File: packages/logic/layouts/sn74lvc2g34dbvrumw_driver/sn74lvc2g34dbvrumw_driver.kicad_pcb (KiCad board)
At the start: 2 copper layers, 2 parts

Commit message: WIP update logic
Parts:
- C1: footprint atopile:C0402-b3ef17 -> Samsung_Electro_Mechanics_CL05B104KO5NNNC:C0402
- U1: footprint atopile:SOT-23-6_L2.9-W1.6-P0.95-LS2.8-BR-bfc73b -> UMW_SN74LVC2G34DBVR_UMW:SOT-23-6_L2.9-W1.6-P0.95-LS2.8-BR
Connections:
- U1 pad 1: line-1 -> line
- U1 pad 4: line-3 -> line-1
- U1 pad 6: line -> line-3
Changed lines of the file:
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@@
     (net 0 "")
     (net 7 "VCC")
-    (net 8 "line-1")
+    (net 8 "line")
     (net 9 "gnd")
-    (net 10 "line")
+    (net 10 "line-3")
     (net 11 "line-2")
-    (net 12 "line-3")
-    (footprint "atopile:C0402-b3ef17"
+    (net 12 "line-1")
+    (footprint "Samsung_Electro_Mechanics_CL05B104KO5NNNC:C0402"
         (layer "F.Cu")
         (at -3.5 0 180)
@@
             )
         )
-        (property "Datasheet" ""
+        (property "Datasheet" "https://www.lcsc.com/datasheet/lcsc_datasheet_2304140030_Samsung-Electro-Mechanics-CL05B104KO5NNNC_C1525.pdf"
             (at 0 0 0)
             (layer "F.Fab")
@@
             )
         )
-        (property "__atopile_lib_fp_hash__" "ef4a2faf-85b3-7ef1-eb8e-b02118ddfcb4"
+        (property "__atopile_lib_fp_hash__" "a8dda1fb-951b-1ec9-ddcd-1be02a19fa0b"
             (at 0 0 0)
             (layer "User.9")
@@
             )
         )
+        (property "checksum" "6defc2b2ec38bb2969880252ed576d3bdeb093dc3bff2a0e0428d940391a2a4b"
+            (at 0 0 0)
+            (layer "User.9")
+            (hide no)
+            (effects
+                (font
+                    (size 0.125 0.125)
+                    (thickness 0.01875)
+                )
+                (hide yes)
+            )
+        )
         (attr smd)
+        (fp_line
+            (start 1.02 -0.5)
+            (end 0.23 -0.5)
+            (stroke
+                (width 0.15)
+                (type solid)
+            )
+            (layer "F.SilkS")
+        )
+        (fp_line
+            (start 0.23 0.5)
+            (end 1.02 0.5)
+            (stroke
+                (width 0.15)
+                (type solid)
+            )
+            (layer "F.SilkS")
+        )
         (fp_line
             (start 1.17 0.35)
@@
         )
         (fp_line
-            (start 1.02 -0.5)
-            (end 0.23 -0.5)
-            (stroke
-                (width 0.15)
-                (type solid)
-            )
-            (layer "F.SilkS")
-        )
-        (fp_line
-            (start 0.23 0.5)
-            (end 1.02 0.5)
+            (start -1.02 -0.5)
+            (end -0.23 -0.5)
             (stroke
                 (width 0.15)
@@
         )
         (fp_line
-            (start -1.02 -0.5)
-            (end -0.23 -0.5)
-            (stroke
-                (width 0.15)
-                (type solid)
-            )
-            (layer "F.SilkS")
-        )
-        (fp_line
             (start -1.17 0.35)
             (end -1.17 -0.35)
@@
         (fp_arc
             (start 1.17 0.35)
-            (mid 1.126066 0.456066)
-            (end 1.02 0.5)
+            (mid 1.1260660171779822 0.456066017177982)
+            (end 1.02 0.4999999999999999)
             (stroke
                 (width 0.15)
@@
         (fp_arc
             (start 1.02 -0.5)
-            (mid 1.126066 -0.456066)
+            (mid 1.1260660171779822 -0.4560660171779821)
             (end 1.17 -0.35)
             (stroke
@@
         )
         (fp_arc
-            (start -1.02 0.5)
-            (mid -1.126066 0.456066)
-            (end -1.17 0.35)
+            (start -1.17 0.35)
+            (mid -1.1260660171779822 0.456066017177982)
+            (end -1.02 0.4999999999999999)
             (stroke
                 (width 0.15)
@@
         )
         (fp_arc
-            (start -1.17 -0.35)
-            (mid -1.126066 -0.456066)
-            (end -1.02 -0.5)
+            (start -1.02 -0.5)
+            (mid -1.1260660171779822 -0.4560660171779821)
+            (end -1.17 -0.35)
             (stroke
                 (width 0.15)
@@
             (layer "F.Fab")
         )
+        (fp_text user "%R"
+            (at 0 0 0)
+            (layer "F.Fab")
+            (effects
+                (font
+                    (size 1 1)
+                    (thickness 0.15)
+                )
+            )
+            (unlocked no)
+        )
         (fp_text user "${REFERENCE}"
-            (at 0 0 0)
-            (layer "F.Fab")
+            (at 0 -4 0)
+            (layer "F.SilkS")
             (effects
                 (font
@@
             )
             (unlocked no)
+        )
+        (pad "2" smd rect
+            (at 0.55 0 180)
+            (size 0.79 0.54)
+            (layers "F.Cu" "F.Paste" "F.Mask")
+            (net 9 "gnd")
         )
         (pad "1" smd rect
             (at -0.55 0 180)
             (size 0.79 0.54)
-            (layers "F.Cu" "F.Mask" "F.Paste")
+            (layers "F.Cu" "F.Paste" "F.Mask")
             (net 7 "VCC")
         )
-        (pad "2" smd rect
-            (at 0.55 0 180)
-            (size 0.79 0.54)
-            (layers "F.Cu" "F.Mask" "F.Paste")
-            (net 9 "gnd")
-        )
-        (embedded_fonts no)
+        (model "${KIPRJMOD}/../../parts/Samsung_Electro_Mechanics_CL05B104KO5NNNC/C0402_L1.0-W0.5-H0.5.step"
+            (offset
+                (xyz 0 0 0)
+            )
+            (scale
+                (xyz 1 1 1)
+            )
+            (rotate
+                (xyz 0 0 0)
+            )
+        )
     )
-    (footprint "atopile:SOT-23-6_L2.9-W1.6-P0.95-LS2.8-BR-bfc73b"
+    (footprint "UMW_SN74LVC2G34DBVR_UMW:SOT-23-6_L2.9-W1.6-P0.95-LS2.8-BR"
         (layer "F.Cu")
         (at 0 0 0)
@@
                     (thickness 0.15)
                 )
-                (hide yes)
             )
         )
@@
             )
         )
-        (property "__atopile_lib_fp_hash__" "7cd08ec5-0e67-1657-3d93-8dff281e4252"
+        (property "__atopile_lib_fp_hash__" "1349fb2a-c60f-22cc-0534-77da642b2d35"
             (at 0 0 0)
             (layer "User.9")
@@
                     (thickness 0.01875)
                 )
+            )
+        )
+        (property "checksum" "90c74f2781f446a0c322669d965f531dd418a618657f545bd3f6b8b0b60fa378"
+            (at 0 0 0)
+            (layer "User.9")
+            (hide no)
+            (effects
+                (font
+                    (size 0.125 0.125)
+                    (thickness 0.01875)
+                )
+                (hide yes)
             )
         )
@@
             (size 1.1 0.6)
             (layers "F.Cu" "F.Paste" "F.Mask")
-            (net 8 "line-1")
+            (net 8 "line")
         )
         (pad "6" smd rect
@@
             (size 1.1 0.6)
             (layers "F.Cu" "F.Paste" "F.Mask")
-            (net 10 "line")
+            (net 10 "line-3")
         )
         (pad "5" smd rect
@@
             (size 1.1 0.6)
             (layers "F.Cu" "F.Paste" "F.Mask")
-            (net 12 "line-3")
-        )
-        (model "/home/ruben/Documents/repos/atopile_projects/Apps/ato-library/packages/logic/build/kicad/libs/lcsc.3dshapes/SOT-23-6_L2.9-W1.6-H1.5-LS2.8-P0.95.wrl"
+            (net 12 "line-1")
+        )
+        (model "${KIPRJMOD}/../../parts/UMW_SN74LVC2G34DBVR_UMW/SOT-23-6_L2.9-W1.6-H1.5-LS2.8-P0.95.step"
             (offset
                 (xyz 0 0 0)

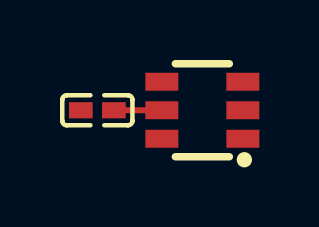
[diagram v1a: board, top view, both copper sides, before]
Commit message: Update 3D model locations
fix missing renders
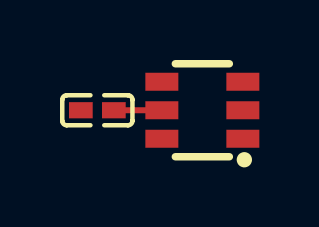
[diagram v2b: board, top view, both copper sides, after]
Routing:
- net VCC: track 0.00 -> 1.60 mm
- net (no net): track 1.60 -> 0.00 mm

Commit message: rebuild all packages & regenerate images of changed layouts (silk)
Add new scripts for version bump and build (based on atopile/packages)
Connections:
- U1 pad 3: line-2 -> line-1
- U1 pad 4: line-1 -> line-3
- U1 pad 6: line-3 -> line-2
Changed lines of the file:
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@@
     (net 2 "line")
     (net 3 "gnd")
-    (net 4 "line-3")
-    (net 5 "line-2")
-    (net 6 "line-1")
+    (net 4 "line-2")
+    (net 5 "line-1")
+    (net 6 "line-3")
     (footprint "UMW_SN74LVC2G34DBVR_UMW:SOT-23-6_L2.9-W1.6-P0.95-LS2.8-BR"
         (layer "F.Cu")
@@
             )
         )
-        (property "__atopile_lib_fp_hash__" "1349fb2a-c60f-22cc-0534-77da642b2d35"
+        (property "__atopile_lib_fp_hash__" "50ac2c3c-bf16-be49-574d-6dfde1c4a470"
             (at 0 0 0)
             (layer "User.9")
@@
             )
         )
-        (property "checksum" "90c74f2781f446a0c322669d965f531dd418a618657f545bd3f6b8b0b60fa378"
-            (at 0 0 0)
-            (layer "User.9")
-            (hide yes)
-            (effects
-                (font
-                    (size 0.125 0.125)
-                    (thickness 0.01875)
-                )
+        (property "checksum" "6bc27c223c43a0951c7a317be577427d2176831fcb6a64a0bd8550f595544d12"
+            (at 0 0 0)
+            (layer "User.9")
+            (hide no)
+            (effects
+                (font
+                    (size 0.125 0.125)
+                    (thickness 0.01875)
+                )
+                (hide yes)
             )
         )
@@
         )
         (fp_circle
-            (center 1.4 1.65)
-            (end 1.53 1.65)
-            (stroke
-                (width 0.25)
+            (center 1.4 1.45)
+            (end 1.43 1.45)
+            (stroke
+                (width 0.06)
                 (type solid)
             )
             (fill no)
-            (layer "F.SilkS")
+            (layer "F.Fab")
         )
         (fp_circle
@@
         )
         (fp_circle
-            (center 1.4 1.45)
-            (end 1.43 1.45)
-            (stroke
-                (width 0.06)
+            (center 1.4 1.65)
+            (end 1.53 1.65)
+            (stroke
+                (width 0.25)
                 (type solid)
             )
             (fill no)
-            (layer "F.Fab")
+            (layer "F.SilkS")
+        )
+        (fp_text user "%R"
+            (at 0 0 0)
+            (layer "F.Fab")
+            (effects
+                (font
+                    (size 1 1)
+                    (thickness 0.15)
+                )
+            )
+            (unlocked no)
         )
         (fp_text user "${REFERENCE}"
-            (at 0 0 0)
-            (layer "F.Fab")
+            (at 0 -4.95 0)
+            (layer "F.SilkS")
             (effects
                 (font
@@
             )
             (unlocked no)
+        )
+        (pad "3" smd rect
+            (at 1.35 -0.95 0)
+            (size 1.1 0.6)
+            (layers "F.Cu" "F.Paste" "F.Mask")
+            (net 5 "line-1")
+        )
+        (pad "2" smd rect
+            (at 1.35 0 0)
+            (size 1.1 0.6)
+            (layers "F.Cu" "F.Paste" "F.Mask")
+            (net 3 "gnd")
         )
         (pad "1" smd rect
             (at 1.35 0.95 0)
             (size 1.1 0.6)
-            (layers "F.Cu" "F.Mask" "F.Paste")
+            (layers "F.Cu" "F.Paste" "F.Mask")
             (net 2 "line")
         )
-        (pad "2" smd rect
-            (at 1.35 0 0)
-            (size 1.1 0.6)
-            (layers "F.Cu" "F.Mask" "F.Paste")
-            (net 3 "gnd")
-        )
-        (pad "3" smd rect
-            (at 1.35 -0.95 0)
-            (size 1.1 0.6)
-            (layers "F.Cu" "F.Mask" "F.Paste")
-            (net 5 "line-2")
+        (pad "6" smd rect
+            (at -1.35 0.95 0)
+            (size 1.1 0.6)
+            (layers "F.Cu" "F.Paste" "F.Mask")
+            (net 4 "line-2")
+        )
+        (pad "5" smd rect
+            (at -1.35 0 0)
+            (size 1.1 0.6)
+            (layers "F.Cu" "F.Paste" "F.Mask")
+            (net 1 "VCC")
         )
         (pad "4" smd rect
             (at -1.35 -0.95 0)
             (size 1.1 0.6)
-            (layers "F.Cu" "F.Mask" "F.Paste")
-            (net 6 "line-1")
-        )
-        (pad "5" smd rect
-            (at -1.35 0 0)
-            (size 1.1 0.6)
-            (layers "F.Cu" "F.Mask" "F.Paste")
-            (net 1 "VCC")
-        )
-        (pad "6" smd rect
-            (at -1.35 0.95 0)
-            (size 1.1 0.6)
-            (layers "F.Cu" "F.Mask" "F.Paste")
-            (net 4 "line-3")
-        )
-        (embedded_fonts no)
+            (layers "F.Cu" "F.Paste" "F.Mask")
+            (net 6 "line-3")
+        )
         (model "${KIPRJMOD}/../../parts/UMW_SN74LVC2G34DBVR_UMW/SOT-23-6_L2.9-W1.6-H1.5-LS2.8-P0.95.step"
             (offset
